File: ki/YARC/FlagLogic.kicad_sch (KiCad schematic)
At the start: 0 parts

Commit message: Schematic for flags. Also ongoing improvements to register test (as yet incomplete)
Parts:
- added U? (x5): 74LS86, symbol 74xx:74LS86
- added U? (x5): 74LS32, symbol 74xx:74LS32
- added U? (x2): 74LS573, symbol 74xx:74LS573
- added U? (x5): 74HC00, symbol 74xx:74HC00
- added U? (x3): 74LS21, symbol 74xx:74LS21
- added U? (x3): 74LS139, symbol 74xx:74LS139
- added U?: 74LS153, symbol 74xx:74LS153
- added U? (x2): 74LS574, symbol 74xx:74LS574
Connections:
- new net: U?.4, U?.6
- new net: U?.2 (A0), U?.6
- new net: U?.3, U?.5 (I1a)
- new net: U?.1, U?.2, U?.3, U?.4, U?.4 (I2a)
- new net: U?.10, U?.5 (O1)
- new net: U?.12, U?.13, U?.7 (O3)
- new net: U?.4 (O0), U?.9
- new net: U?.3 (I3a), U?.6
- new net: U?.1 (Ea), U?.3
- new net: U?.4, U?.7 (Za)
- new net: U?.5, U?.9 (Zb)
- new net GND: U?.10, U?.10, U?.10, U?.12, U?.12, U?.12, U?.13, U?.13, U?.13, U?.13 (A1), U?.14 (A0), U?.15 (E), U?.4, U?.5, U?.7 (GND), U?.7 (GND), U?.7 (GND), U?.7 (GND), U?.8 (GND), U?.8 (GND), U?.9, U?.9, U?.9
- new net IRH0: U?.14 (S0)
- new net IRH1: U?.2 (S1)
- new net IRH2: U?.1, U?.15 (Eb), U?.2
- new net IRH3: U?.5
- new net REG_C: U?.1, U?.10 (I0b)
- new net REG_N: U?.1, U?.12 (I2b), U?.5
- new net REG_V: U?.13 (I3b), U?.2
- new net REG_Z: U?.11 (I1b), U?.2
- new net RSW2: U?.3 (A1)
- new net VCC: U?.14 (VCC), U?.14 (VCC), U?.14 (VCC), U?.14 (VCC), U?.16 (VCC), U?.16 (VCC), U?.6 (I0a)
- new net ~{dst_clk_en}: U?.8
- new net ~{dst_wr_en}: U?.1 (E)
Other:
- note added: "FLAGS LOGIC"
- note added: "UNUSED GATES"

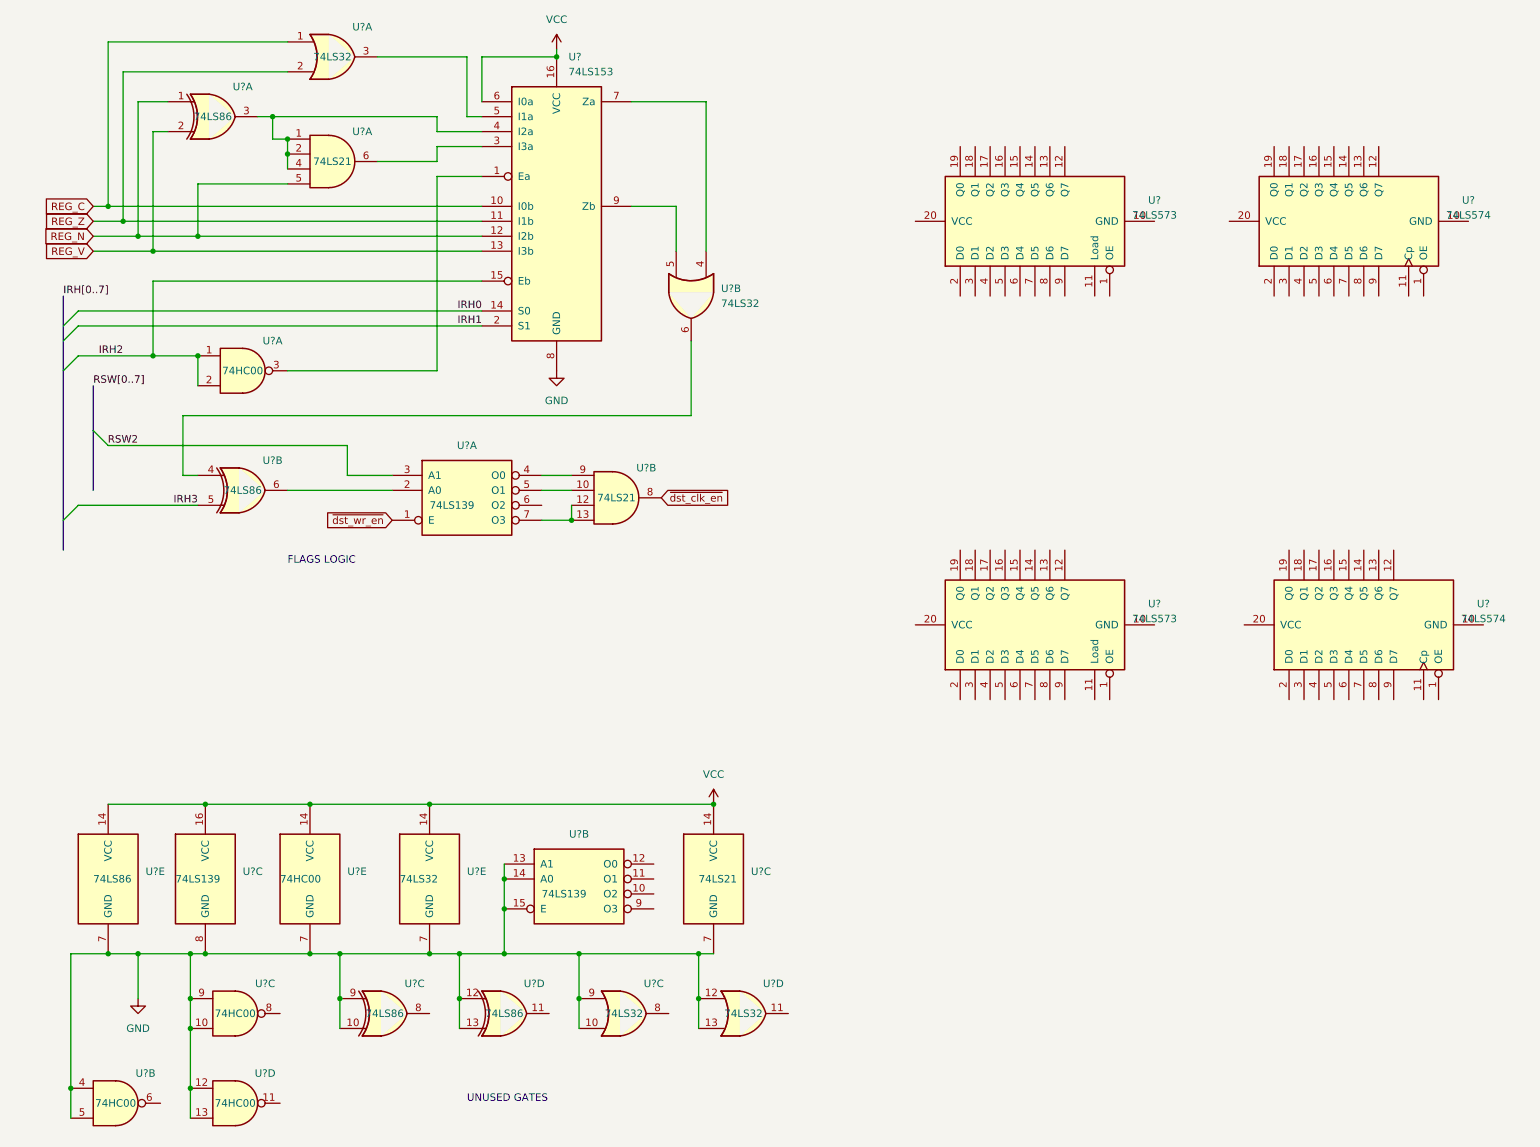
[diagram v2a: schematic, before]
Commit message: Major changes to ALU, Flags, and add new ALU controls schematic
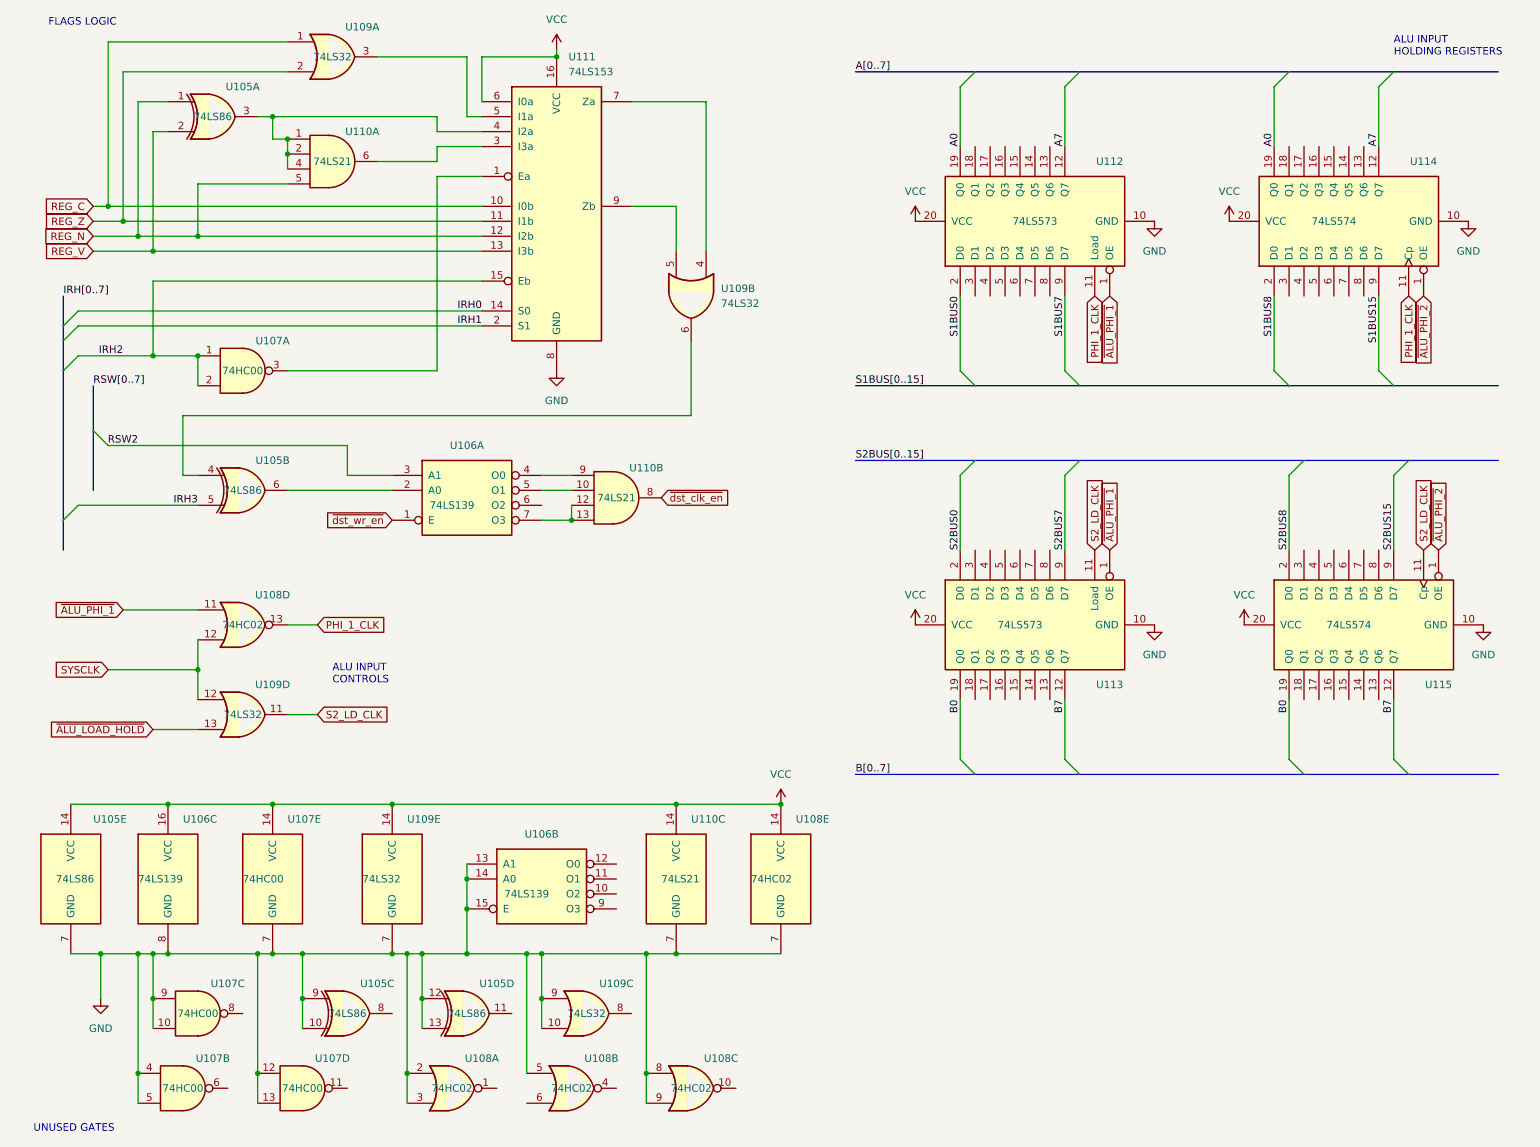
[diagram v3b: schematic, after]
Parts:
- added U108: 74HC02, symbol 74xx:74HC02
- gave numbers to parts that had none: 10
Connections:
- net GND: now also U112.10 (GND), U113.10 (GND), U114.10 (GND), U115.10 (GND), U108.2, U108.3, U108.5, U108.7 (GND), U108.8, U108.9; no longer U109.12, U109.13
- net VCC: now also U112.20 (VCC), U113.20 (VCC), U114.20 (VCC), U115.20 (VCC), U108.14 (VCC)
- net ~{ALU_PHI_1}: now reaches U112.1 (OE)
- net ~{ALU_PHI_1}: now also U113.1 (OE), U108.11
- net PHI_1_CLK: now reaches U112.11 (Load)
- net PHI_1_CLK: now also U114.11 (Cp), U108.13
- net A7: now reaches U112.12 (Q7)
- net A7: now also U114.12 (Q7)
- net A0: now reaches U112.19 (Q0)
- net A0: now also U114.19 (Q0)
- net S1BUS0: now reaches U112.2 (D0)
- net S1BUS7: now reaches U112.9 (D7)
- net S2_LD_CLK: now reaches U109.11
- net S2_LD_CLK: now also U113.11 (Load), U115.11 (Cp)
- net ~{ALU_PHI_2}: now reaches U114.1 (OE)
- net ~{ALU_PHI_2}: now also U115.1 (OE)
- net S1BUS8: now reaches U114.2 (D0)
- net S1BUS15: now reaches U114.9 (D7)
- net B7: now reaches U113.12 (Q7)
- net B7: now also U115.12 (Q7)
- net B0: now reaches U113.19 (Q0)
- net B0: now also U115.19 (Q0)
- net S2BUS0: now reaches U113.2 (D0)
- net S2BUS7: now reaches U113.9 (D7)
- net S2BUS8: now reaches U115.2 (D0)
- net S2BUS15: now reaches U115.9 (D7)
- new net SYSCLK: U108.12, U109.12
- new net ~{ALU_LOAD_HOLD}: U109.13
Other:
- note added: "ALU INPUT CONTROLS"
- note added: "ALU INPUT HOLDING REGISTERS"
- moved on the sheet: U105C, U105D, U105E, U106B, U106C, U107B, U107C, U107D, U107E, U109C, U109D, U109E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

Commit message: Believable ALU/Flags design almost complete
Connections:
- net REG_C renamed FREG.C
- net REG_N renamed FREG.N
- net REG_V renamed FREG.V
- net REG_Z renamed FREG.Z
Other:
- moved on the sheet: U105A, U105B, U106A, U107A, U109A, U109B, U110A, U110B, U111

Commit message: Further development of ALU controls
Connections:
- net GND: now also U108.6
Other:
- note added: "ALU INPUT AND OUTPUT CONTROLS"
- note added: "PHI_1_CLK IS ACTIVE HIGH"
- note removed: "ALU INPUT CONTROLS"
- moved on the sheet: U109C
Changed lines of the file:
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@@
   (junction (at 50.8 193.04) (diameter 0) (color 0 0 0 0)
   )
-  (junction (at 99.06 180.34) (diameter 0) (color 0 0 0 0)
-  )
   (junction (at 121.92 172.72) (diameter 0) (color 0 0 0 0)
   )
@@
   (junction (at 45.72 71.12) (diameter 0) (color 0 0 0 0)
   )
-  (junction (at 99.06 172.72) (diameter 0) (color 0 0 0 0)
+  (junction (at 96.52 193.04) (diameter 0) (color 0 0 0 0)
   )
   (junction (at 38.1 53.34) (diameter 0) (color 0 0 0 0)
@@
   (junction (at 50.8 172.72) (diameter 0) (color 0 0 0 0)
   )
+  (junction (at 96.52 185.42) (diameter 0) (color 0 0 0 0)
+  )
   (junction (at 76.2 193.04) (diameter 0) (color 0 0 0 0)
   )
@@
   (junction (at 139.7 147.32) (diameter 0) (color 0 0 0 0)
   )
+  (junction (at 96.52 180.34) (diameter 0) (color 0 0 0 0)
+  )
   (junction (at 60.96 34.29) (diameter 0) (color 0 0 0 0)
   )
@@
     (stroke (width 0) (type default) (color 0 0 0 0))
   )
-  (wire (pts (xy 99.06 172.72) (xy 116.84 172.72))
-    (stroke (width 0) (type default) (color 0 0 0 0))
-  )
   (wire (pts (xy 25.4 124.46) (xy 40.64 124.46))
     (stroke (width 0) (type default) (color 0 0 0 0))
@@
     (stroke (width 0) (type default) (color 0 0 0 0))
   )
+  (wire (pts (xy 96.52 180.34) (xy 96.52 172.72))
+    (stroke (width 0) (type default) (color 0 0 0 0))
+  )
   (wire (pts (xy 129.54 81.28) (xy 43.18 81.28))
     (stroke (width 0) (type default) (color 0 0 0 0))
@@
     (stroke (width 0) (type default) (color 0 0 0 0))
   )
-  (wire (pts (xy 99.06 185.42) (xy 99.06 180.34))
-    (stroke (width 0) (type default) (color 0 0 0 0))
-  )
   (wire (pts (xy 45.72 41.91) (xy 45.72 50.8))
     (stroke (width 0) (type default) (color 0 0 0 0))
@@
     (stroke (width 0) (type default) (color 0 0 0 0))
   )
+  (wire (pts (xy 96.52 185.42) (xy 96.52 180.34))
+    (stroke (width 0) (type default) (color 0 0 0 0))
+  )
   (bus (pts (xy 226.06 22.86) (xy 243.84 22.86))
     (stroke (width 0) (type default) (color 0 0 0 0))
@@
     (stroke (width 0) (type default) (color 0 0 0 0))
   )
-  (wire (pts (xy 96.52 172.72) (xy 99.06 172.72))
+  (wire (pts (xy 96.52 172.72) (xy 116.84 172.72))
     (stroke (width 0) (type default) (color 0 0 0 0))
   )
@@
     (stroke (width 0) (type default) (color 0 0 0 0))
   )
+  (wire (pts (xy 96.52 193.04) (xy 96.52 185.42))
+    (stroke (width 0) (type default) (color 0 0 0 0))
+  )
   (bus (pts (xy 226.06 76.2) (xy 243.84 76.2))
     (stroke (width 0) (type default) (color 0 0 0 0))
@@
     (stroke (width 0) (type default) (color 0 0 0 0))
   )
-  (wire (pts (xy 99.06 180.34) (xy 99.06 172.72))
-    (stroke (width 0) (type default) (color 0 0 0 0))
-  )
   (bus (pts (xy 22.86 60.96) (xy 22.86 66.04))
     (stroke (width 0) (type default) (color 0 0 0 0))
@@
     (stroke (width 0) (type default) (color 0 0 0 0))
   )
+  (wire (pts (xy 96.52 198.12) (xy 96.52 193.04))
+    (stroke (width 0) (type default) (color 0 0 0 0))
+  )
   (bus (pts (xy 15.24 53.34) (xy 15.24 55.88))
     (stroke (width 0) (type default) (color 0 0 0 0))
@@
     (stroke (width 0) (type default) (color 0 0 0 0))
   )
-  (wire (pts (xy 96.52 193.04) (xy 96.52 172.72))
-    (stroke (width 0) (type default) (color 0 0 0 0))
-  )
   (wire (pts (xy 38.1 53.34) (xy 93.98 53.34))
     (stroke (width 0) (type default) (color 0 0 0 0))
@@
     (stroke (width 0) (type default) (color 0 0 0 0))
   )
-  (text "ALU INPUT\nCONTROLS" (at 63.5 127 0)
+  (text "ALU INPUT AND\nOUTPUT CONTROLS" (at 60.96 127 0)
     (effects (font (size 1.27 1.27)) (justify left bottom))
   )
@@
   )
   (text "FLAGS LOGIC" (at 20.32 15.24 0)
+    (effects (font (size 1.27 1.27)) (justify left bottom))
+  )
+  (text "PHI_1_CLK IS\nACTIVE HIGH" (at 60.96 114.3 0)
     (effects (font (size 1.27 1.27)) (justify left bottom))
   )
@@
     (pin "9")
   )
-  (symbol (lib_id "74xx:74LS32") (at 106.68 182.88 0) (unit 3)
-    (in_bom yes) (on_board yes)
-    (property "Reference" "U109" (id 0) (at 111.76 177.8 0))
-    (property "Value" "74LS32" (id 1) (at 106.68 182.88 0))
-    (property "Footprint" "" (id 2) (at 106.68 182.88 0)
-      (effects (font (size 1.27 1.27)) hide)
-    )
-    (property "Datasheet" "http://www.ti.com/lit/gpn/sn74LS32" (id 3) (at 106.68 182.88 0)
-      (effects (font (size 1.27 1.27)) hide)
-    )
+  (symbol (lib_id "74xx:74LS32") (at 104.14 182.88 0) (unit 3)
+    (in_bom yes) (on_board yes)
+    (property "Reference" "U109" (id 0) (at 109.22 177.8 0))
+    (property "Value" "74LS32" (id 1) (at 104.14 182.88 0))
+    (property "Footprint" "" (id 2) (at 104.14 182.88 0)
+      (effects (font (size 1.27 1.27)) hide)
+    )
+    (property "Datasheet" "http://www.ti.com/lit/gpn/sn74LS32" (id 3) (at 104.14 182.88 0)
+      (effects (font (size 1.27 1.27)) hide)
+    )

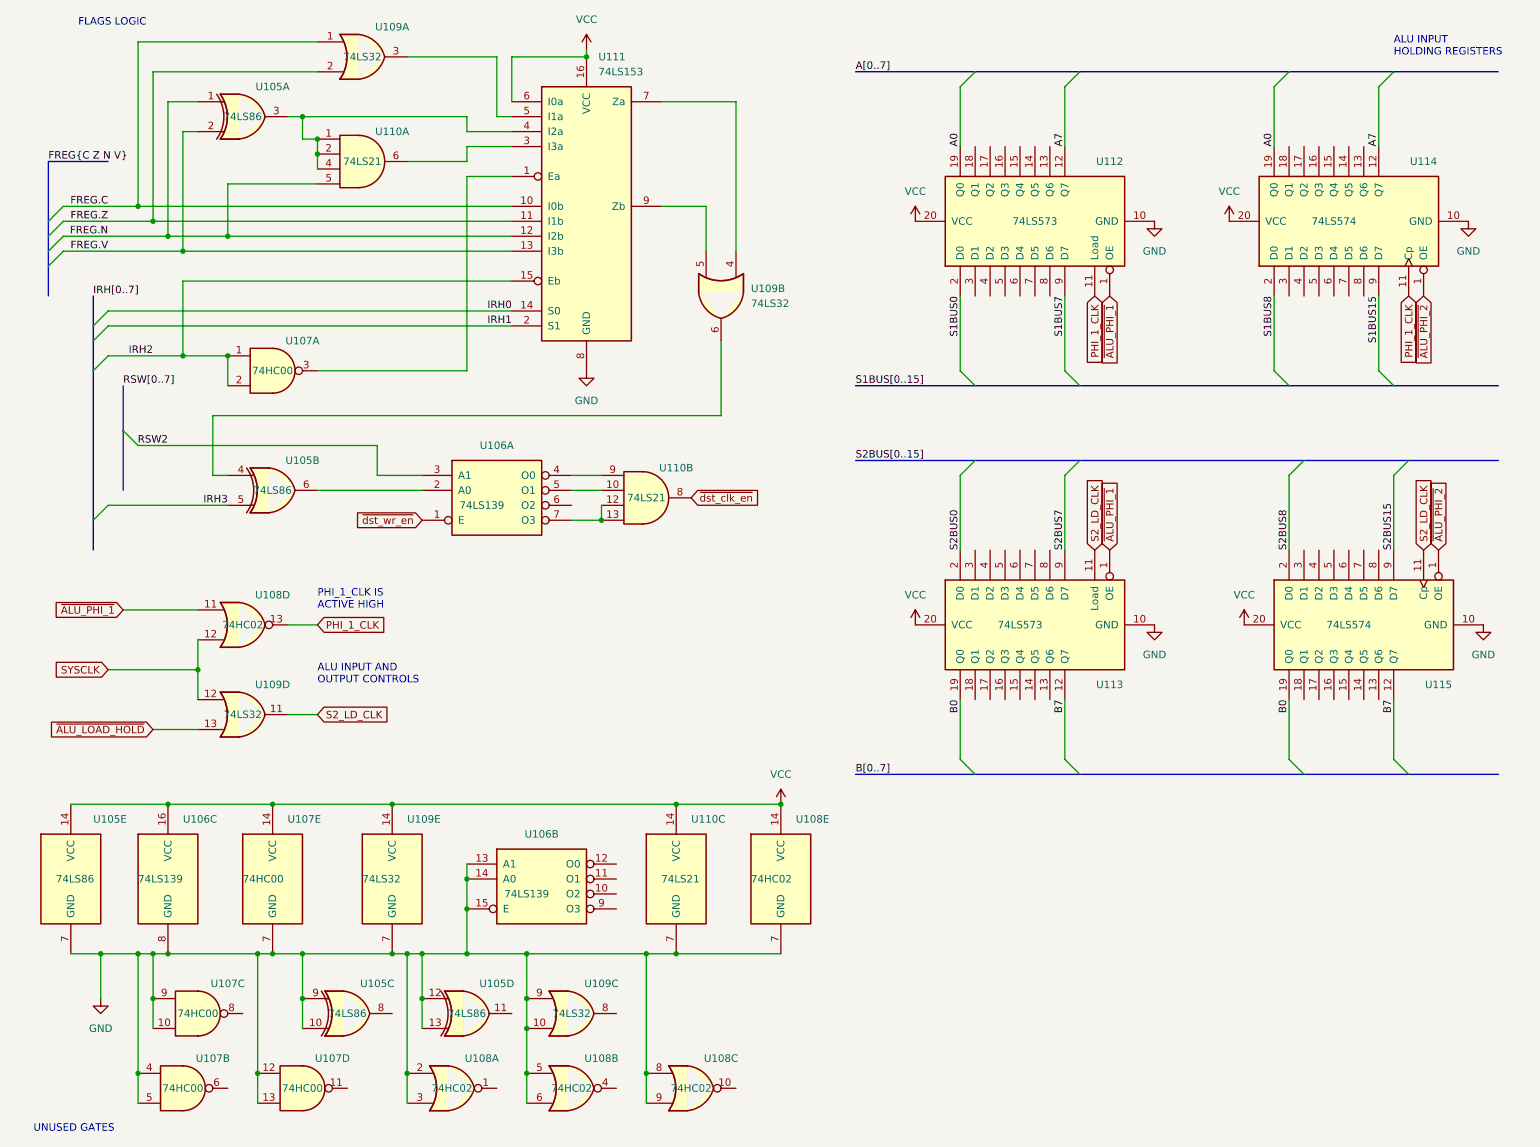
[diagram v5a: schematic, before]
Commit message: ALU schematic checking complete. Ready to start layout.
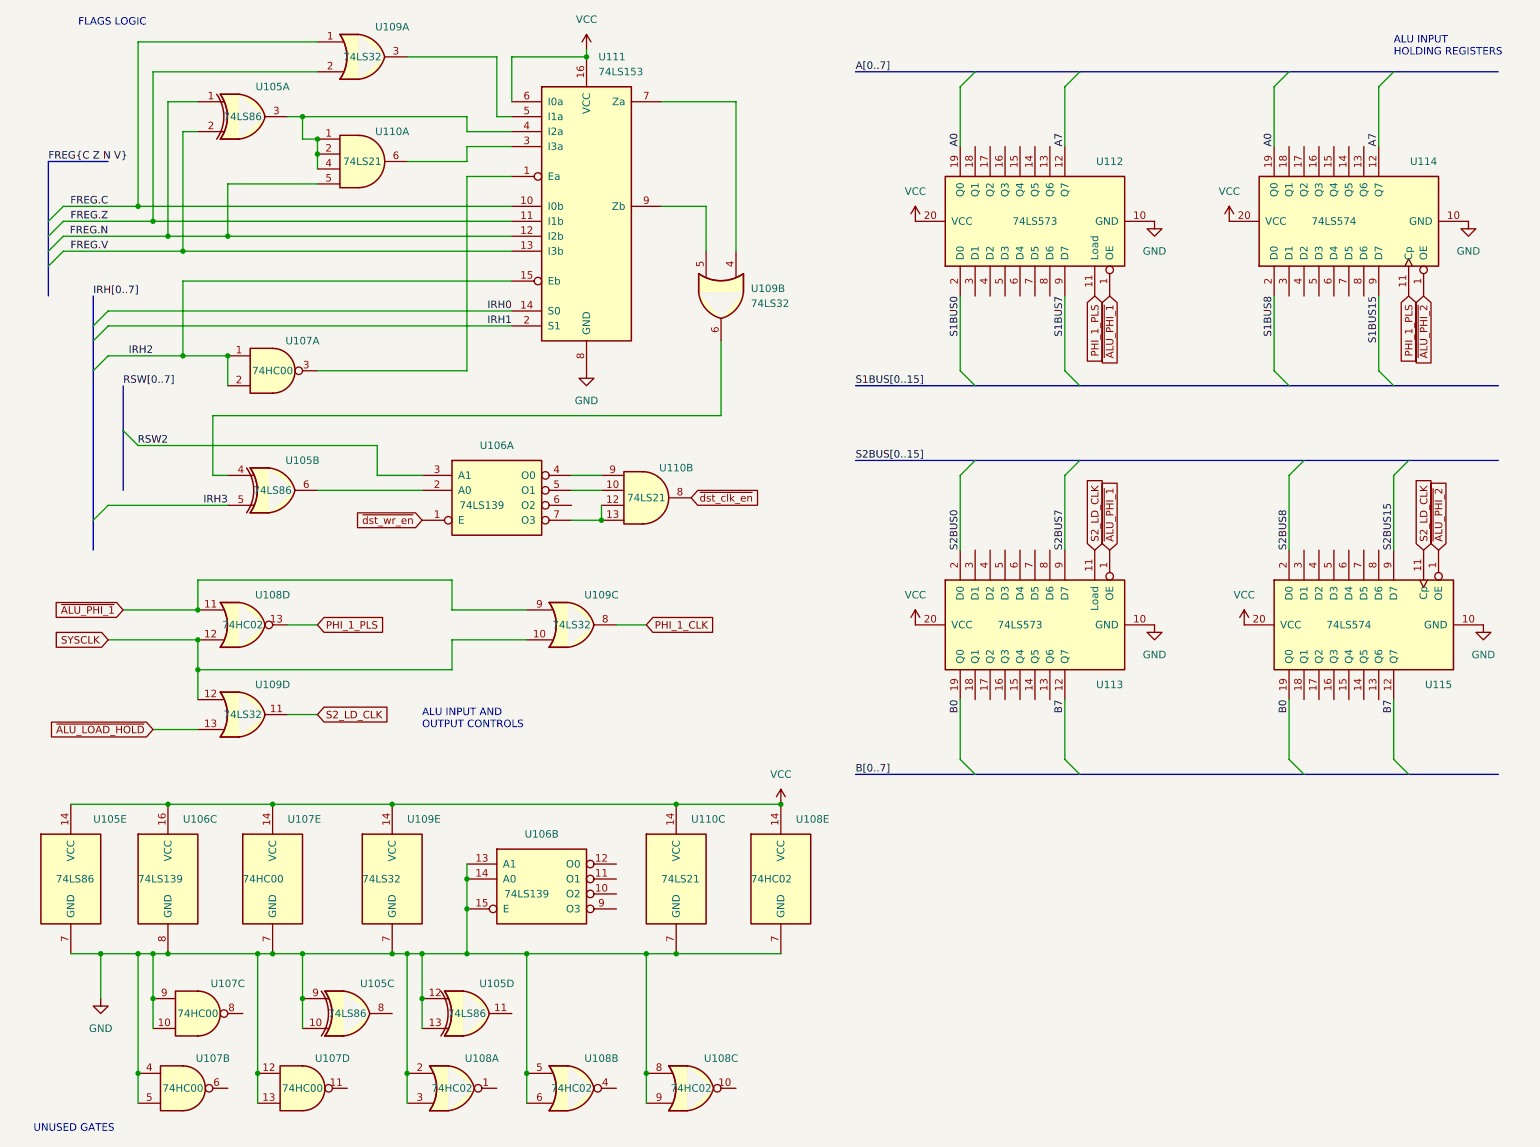
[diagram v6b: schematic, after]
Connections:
- net GND: no longer U109.10, U109.9
- net PHI_1_CLK: now also U109.8; no longer U108.13, U112.11 (Load), U114.11 (Cp)
- net SYSCLK: now also U109.10
- net ~{ALU_PHI_1}: now also U109.9
- new net PHI_1_PLS: U108.13, U112.11 (Load), U114.11 (Cp)
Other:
- note removed: "PHI_1_CLK IS ACTIVE HIGH"
- moved on the sheet: U109C
